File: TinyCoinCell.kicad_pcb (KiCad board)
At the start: 4 copper layers, 23.8 x 24 mm, 35 parts, among them SW1 SW_Push, U1 nRF54L15-QFAA, X1 32MHz, X2 32.768kHz

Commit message: Updated with BOM
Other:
- board text added: "1.09"
- board text added: "1.10"
- board text added: "CLK"
- board text added: "DIO"
- board text added: "GND"
- board text added: "VDD"
- board text added: "~{RST}"

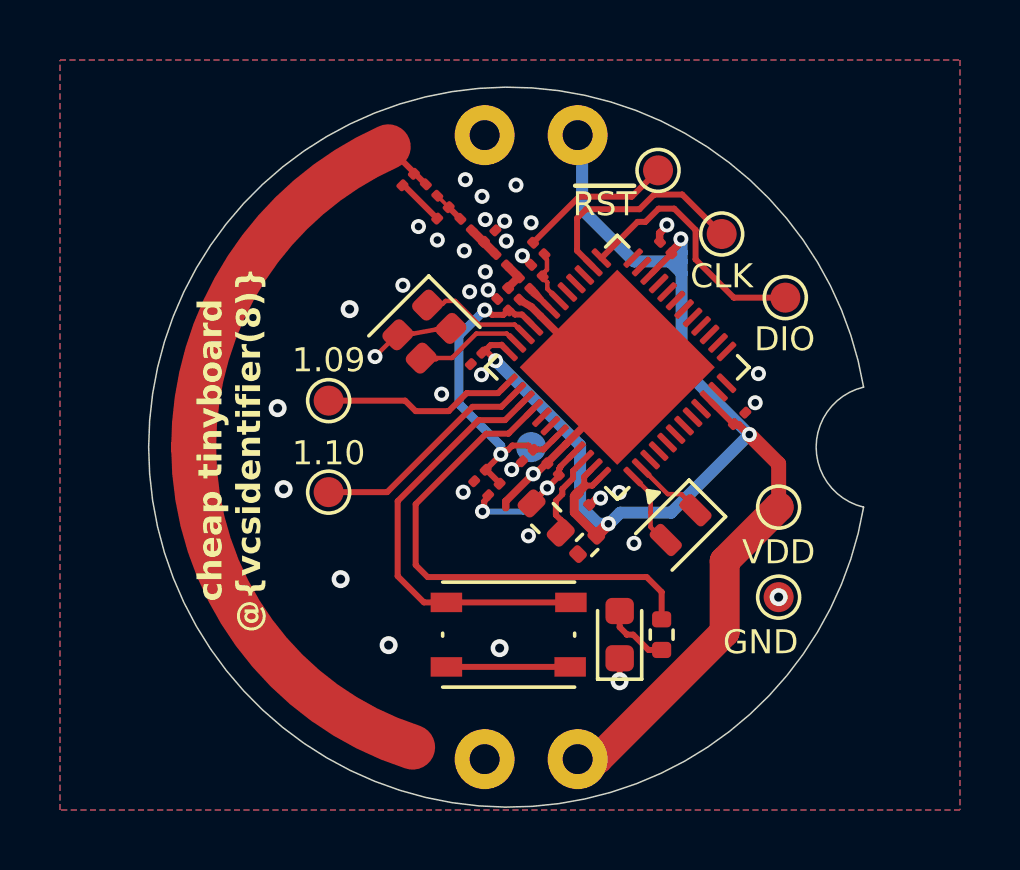
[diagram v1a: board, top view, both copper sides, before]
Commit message: Updates for nPM2100
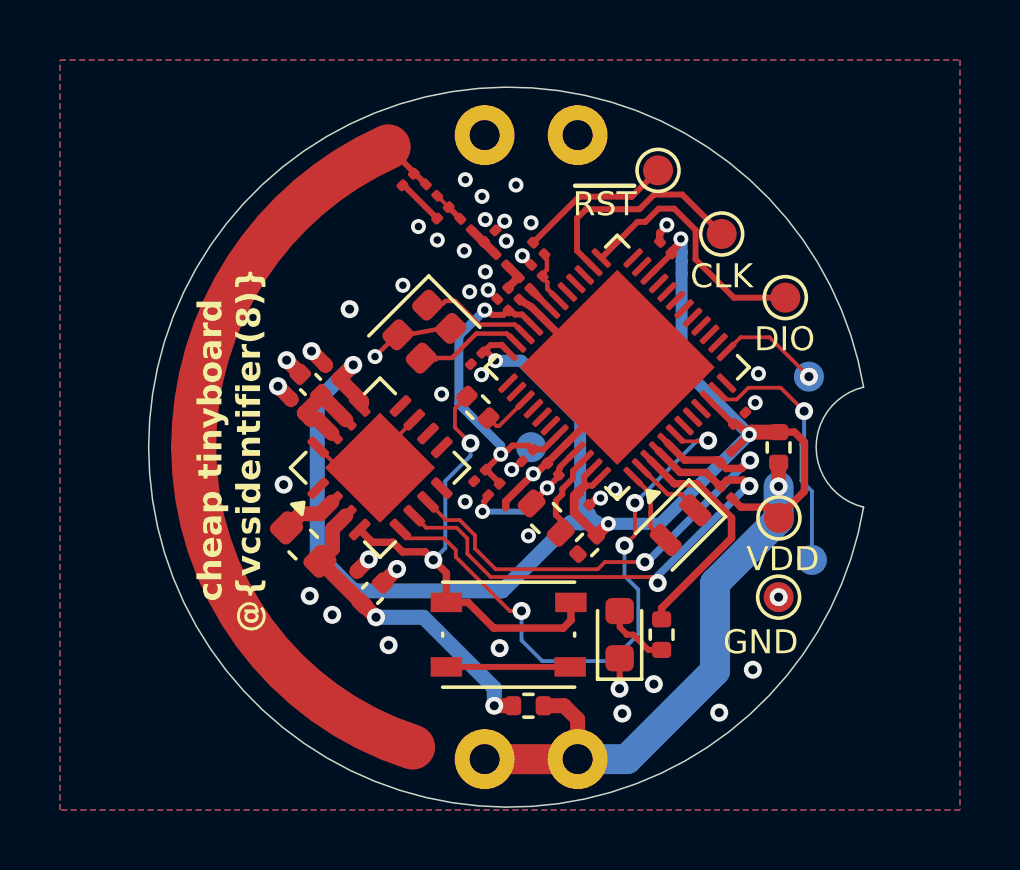
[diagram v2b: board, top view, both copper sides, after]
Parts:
- added C44: 10uF, Capacitor_SMD:C_0402_1005Metric, F.Cu at (139.3, 117.0)
- added C45: 1uF, Capacitor_SMD:C_0201_0603Metric, F.Cu at (138.5, 116.5)
- added C46: 22uF, Capacitor_SMD:C_0402_1005Metric, F.Cu at (137.2, 110.0)
- added C47: 1uF, Capacitor_SMD:C_0201_0603Metric, F.Cu at (136.8, 110.7)
- added C49: 2.2uF, Capacitor_SMD:C_0201_0603Metric, F.Cu at (137.9, 109.6)
- added L6: 2.2uH, Inductor_SMD:L_0603_1608Metric, F.Cu at (136.9, 115.3)
- added R3: 0R, Resistor_SMD:R_0402_1005Metric, F.Cu at (144.5, 120.7)
- added R4: 0R, Resistor_SMD:R_0402_1005Metric, F.Cu at (152.8, 112.1)
- added R5: 1kR, passives:R_0201_0603Metric_L, F.Cu at (151.0, 113.6)
- added R6: 1kR, passives:R_0201_0603Metric_L, F.Cu at (151.0, 112.4)
- added R7: 0R, Resistor_SMD:R_0402_1005Metric, F.Cu at (142.8, 110.8)
- added U8: nPM2100-QEXX, Package_DFN_QFN:UQFN-16-1EP_4x4mm_P0.65mm_EP2.6x2.6mm, F.Cu at (139.5, 112.8)
- TP6, TP7: moved to B.Cu
- moved TP6 17.0 mm to (153.9, 115.9), turned to 180 degrees
- moved TP7 16.5 mm to (153.8, 109.7), turned to 180 degrees
- moved TP4 0.36 mm to (152.8, 114.5)
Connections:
- BT1 pad 1: VDD -> Net-(BT1-+)
- R2 pad 1: Net-(U1-P1.12) -> Net-(U1-P1.02)
- SW1 pad 1: Net-(U1-P1.11) -> /SW1
- TP6 pad 1: Net-(U1-P1.09) -> Net-(U1-P2.00)
- TP7 pad 1: Net-(U1-P1.10) -> Net-(U1-P2.02)
- U1 pad 11: unconnected-(U1-P2.00-Pad11) -> Net-(U1-P2.00)
- U1 pad 13: unconnected-(U1-P2.02-Pad13) -> Net-(U1-P2.02)
- U1 pad 3: unconnected-(U1-P1.02-Pad3) -> Net-(U1-P1.02)
- U1 pad 37: Net-(U1-P1.09) -> unconnected-(U1-P1.09-Pad37)
- U1 pad 38: Net-(U1-P1.10) -> unconnected-(U1-P1.10-Pad38)
- U1 pad 4: unconnected-(U1-P1.03-Pad4) -> /SDA
- U1 pad 40: Net-(U1-P1.12) -> unconnected-(U1-P1.12-Pad40)
- U1 pad 5: unconnected-(U1-P1.04-Pad5) -> /SCL
- U1 pad 6: unconnected-(U1-P1.05-Pad6) -> /nPM2100.GPIO0
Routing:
- net /nPM2100.GPIO0: track 0.00 -> 20.0 mm, vias 0 -> 4
- net Net-(BT1-+): track 0.00 -> 19.4 mm, vias 0 -> 1
- net /SDA: track 0.00 -> 17.6 mm, vias 0 -> 2
- net Net-(U1-P1.12): track 16.8 -> 0.00 mm
- net /SCL: track 0.00 -> 16.7 mm, vias 0 -> 2
- net /SW1: track 0.00 -> 16.0 mm, vias 0 -> 2
- net Net-(U1-P1.11): track 14.3 -> 1.68 mm
- net Net-(U8-VBAT): track 0.00 -> 10.7 mm, vias 0 -> 2
- net Net-(U1-P2.00): track 0.00 -> 8.60 mm, vias 0 -> 1
- net Net-(U1-P1.02): track 0.00 -> 7.86 mm
- net GND: track 17.7 -> 25.6 mm, vias 36 -> 44
- net Net-(U1-P1.10): track 7.65 -> 0.00 mm
- net VDD: track 50.8 -> 57.4 mm, vias 4 -> 5
- net Net-(U1-P1.09): track 6.51 -> 0.00 mm
- net Net-(U1-P2.02): track 0.00 -> 3.48 mm, vias 0 -> 1
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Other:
- board text added: "P2.00"
- board text added: "P2.02"
- board text removed: "1.09"
- board text removed: "1.10"

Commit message: Update for nPM2100, ADXL367
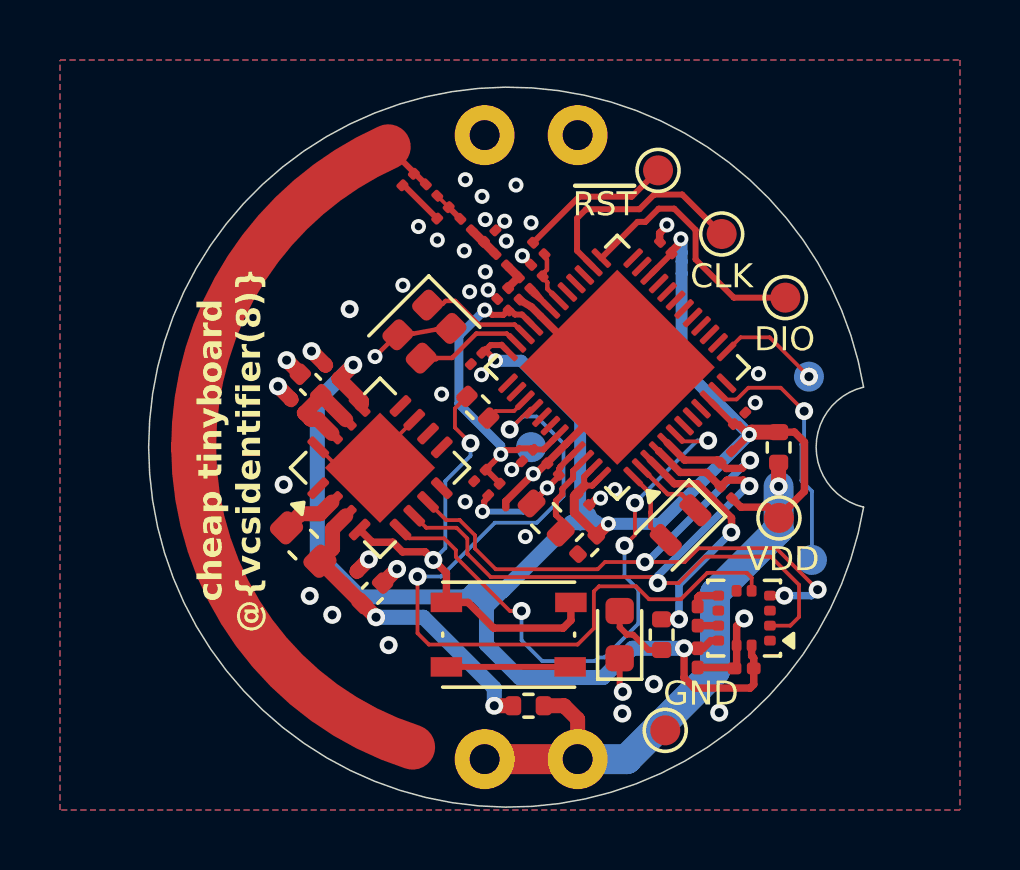
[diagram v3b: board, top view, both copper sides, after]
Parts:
- added C48: 1uF, Capacitor_SMD:C_0201_0603Metric, F.Cu at (150.1, 119.1)
- added C50: 1uF, Capacitor_SMD:C_0201_0603Metric, F.Cu at (151.6, 119.5)
- added C51: 1uF, Capacitor_SMD:C_0201_0603Metric, F.Cu at (150.1, 117.7)
- added U2: ADXL367, TinyCoinCell:ADXL367_LGA-12_2.11x2.21mm_P0.5mm_LayoutBorder2x4y, F.Cu at (151.6, 117.8)
- moved TP5 5.83 mm to (149.0, 121.5)
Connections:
- U1 pad 40: unconnected-(U1-P1.12-Pad40) -> /INT1
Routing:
- net /INT1: track 0.00 -> 26.9 mm, vias 0 -> 2
- net VDD: track 57.4 -> 74.3 mm, vias 5 -> 6
- net /SCL: track 16.7 -> 24.9 mm, vias 2 -> 4
- net /SDA: track 17.6 -> 25.2 mm
- net GND: track 25.6 -> 29.8 mm, vias 44 -> 42
- net Net-(U2-V_{REG_OUT}): track 0.00 -> 0.69 mm
- net Net-(U1-P1.02): track 7.86 -> 8.20 mm, vias 0 -> 2

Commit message: Updates for manufacturing
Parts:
- C14: value 0.3pF -> 1pF
- U1: footprint Package_DFN_QFN:QFN-48-1EP_6x6mm_P0.4mm_EP4.6x4.6mm -> Package_DFN_QFN:QFN-48-1EP_6x6mm_P0.4mm_EP4.6x4.6mm_ThermalVias
- U8: footprint Package_DFN_QFN:UQFN-16-1EP_4x4mm_P0.65mm_EP2.6x2.6mm -> Package_DFN_QFN:UQFN-16-1EP_4x4mm_P0.65mm_EP2.6x2.6mm_ThermalVias
